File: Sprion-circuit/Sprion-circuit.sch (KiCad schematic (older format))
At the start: 0 parts

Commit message: Push, Push, Push
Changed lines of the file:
@@
 $EndDescr
 $Sheet
-S 1250 1500 2850 1250
+S 1400 1500 2850 1250
 U 60E26C28
 F0 "DRV8212" 50
 F1 "DRV8212.sch" 50
-F2 "MD1_IN1" I L 1250 1600 50
-F3 "MD1_IN2" I L 1250 1700 50
-F4 "MD1_OUT1" I R 4100 1600 50
-F5 "MD1_OUT2" I R 4100 1700 50
-F6 "MD1_CS" I L 1250 1800 50
-F7 "MD2_IN1" I L 1250 1950 50
-F8 "MD2_IN2" I L 1250 2050 50
-F9 "MD2_OUT1" I R 4100 1850 50
-F10 "MD2_OUT2" I R 4100 1950 50
-F11 "MD_SUC_IN1" I L 1250 2300 50
-F12 "MD_SUC_IN2" I L 1250 2400 50
-F13 "MD_SUC_OUT1" I R 4100 2100 50
-F14 "MD_SUC_OUT2" I R 4100 2200 50
-F15 "MD2_CS" I L 1250 2150 50
+F2 "MD1_IN1" I L 1400 1600 50
+F3 "MD1_IN2" I L 1400 1700 50
+F4 "MD1_OUT1" O R 4250 1600 50
+F5 "MD1_OUT2" O R 4250 1700 50
+F6 "MD1_CS" I L 1400 1800 50
+F7 "MD2_IN1" I L 1400 1950 50
+F8 "MD2_IN2" I L 1400 2050 50
+F9 "MD2_OUT1" O R 4250 1850 50
+F10 "MD2_OUT2" O R 4250 1950 50
+F11 "MD_SUC_IN1" I L 1400 2300 50
+F12 "MD_SUC_IN2" I L 1400 2400 50
+F13 "MD_SUC_OUT1" O R 4250 2100 50
+F14 "MD_SUC_OUT2" O R 4250 2200 50
+F15 "MD2_CS" I L 1400 2150 50
 $EndSheet
 $Sheet
@@
 F0 "Power" 50
 F1 "Power.sch" 50
-F2 "BAT" I L 1300 3950 50
+F2 "BAT" O L 1300 3950 50
 $EndSheet
 $Sheet

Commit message: wall sensor
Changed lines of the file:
@@
-$EndSheet
-$Sheet
-S 5200 2100 2600 2050
-U 60F363D5
-F0 "STM32f405" 50
-F1 "STM32f405.sch" 50
 $EndSheet
 $Sheet
@@
 F0 "wall_sensor" 50
 F1 "wall_sensor.sch" 50
+F2 "IRLED_SIDE" I L 8850 2900 50
+F3 "IRLED_FRONT" I L 8850 2750 50
+F4 "SENSOR_WALL_FR" O R 10700 2600 50
+F5 "SENSOR_WALL_FL" O R 10700 2750 50
+F6 "SENSOR_WALL_SR" O R 10700 2900 50
+F7 "SENSOR_WALL_SL" O R 10700 3050 50
+$EndSheet
+$Sheet
+S 5200 2100 2600 2050
+U 60F363D5
+F0 "Controller" 50
+F1 "Controller.sch" 50
 $EndSheet
 $EndSCHEMATC

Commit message: :fix　いろいろ
後で書きます
とりあえず寝ます
許してください
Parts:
- added J? (x2): Conn_02x03_Odd_Even, symbol Connector_Generic:Conn_02x03_Odd_Even
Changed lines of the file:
@@
 $Descr A4 11693 8268
 encoding utf-8
-Sheet 1 5
+Sheet 1 6
 Title ""
 Date ""
@@
 Comment4 ""
 $EndDescr
-$Sheet
-S 1400 1500 2850 1250
-U 60E26C28
-F0 "DRV8212" 50
-F1 "DRV8212.sch" 50
-F2 "MD1_IN1" I L 1400 1600 50
-F3 "MD1_IN2" I L 1400 1700 50
-F4 "MD1_OUT1" O R 4250 1600 50
-F5 "MD1_OUT2" O R 4250 1700 50
-F6 "MD1_CS" I L 1400 1800 50
-F7 "MD2_IN1" I L 1400 1950 50
-F8 "MD2_IN2" I L 1400 2050 50
-F9 "MD2_OUT1" O R 4250 1850 50
-F10 "MD2_OUT2" O R 4250 1950 50
-F11 "MD_SUC_IN1" I L 1400 2300 50
-F12 "MD_SUC_IN2" I L 1400 2400 50
-F13 "MD_SUC_OUT1" O R 4250 2100 50
-F14 "MD_SUC_OUT2" O R 4250 2200 50
-F15 "MD2_CS" I L 1400 2150 50
-$EndSheet
 $Sheet
 S 1300 3750 2100 1200
@@
 F7 "SENSOR_WALL_SL" O R 10700 3050 50
 $EndSheet
+$Comp
+L Connector_Generic:Conn_02x03_Odd_Even J?
+U 1 1 61A7CC1C
+P 5200 1050
+F 0 "J?" V 5204 1230 50  0000 L CNN
+F 1 "Conn_02x03_Odd_Even" V 5295 1230 50  0000 L CNN
+F 2 "" H 5200 1050 50  0001 C CNN
+F 3 "~" H 5200 1050 50  0001 C CNN
+	1    5200 1050
+	0    1    1    0
+$EndComp
+$Comp
+L Connector_Generic:Conn_02x03_Odd_Even J?
+U 1 1 61A7F0D6
+P 6600 1050
+F 0 "J?" V 6604 1230 50  0000 L CNN
+F 1 "Conn_02x03_Odd_Even" V 6695 1230 50  0000 L CNN
+F 2 "" H 6600 1050 50  0001 C CNN
+F 3 "~" H 6600 1050 50  0001 C CNN
+	1    6600 1050
+	0    1    1    0
+$EndComp
 $Sheet
-S 5200 2100 2600 2050
+S 1600 1850 2850 1250
+U 60E26C28
+F0 "DRV8212" 50
+F1 "DRV8212.sch" 50
+F2 "MD1_IN1" I L 1600 1950 50
+F3 "MD1_IN2" I L 1600 2050 50
+F4 "MD1_OUT1" O R 4450 1950 50
+F5 "MD1_OUT2" O R 4450 2050 50
+F6 "MD1_CS" I L 1600 2150 50
+F7 "MD2_IN1" I L 1600 2300 50
+F8 "MD2_IN2" I L 1600 2400 50
+F9 "MD2_OUT1" O R 4450 2200 50
+F10 "MD2_OUT2" O R 4450 2300 50
+F11 "MD_SUC_IN1" I L 1600 2650 50
+F12 "MD_SUC_IN2" I L 1600 2750 50
+F15 "MD2_CS" I L 1600 2500 50
+$EndSheet
+$Sheet
+S 5200 2050 2600 2050
 U 60F363D5
 F0 "Controller" 50
 F1 "Controller.sch" 50
+F2 "IMU_SCK" O R 7800 2150 50
+F3 "IMU_MISO" I R 7800 2250 50
+F4 "IMU_MOSI" O R 7800 2350 50
+F5 "ENCODER_1B" I R 7800 2600 50
+F6 "ENCODER_1A" I R 7800 2700 50
+F7 "IMU_CS" O R 7800 2450 50
+F8 "BATT" I R 7800 3000 50
+F9 "IRLED_FRONT" O R 7800 3200 50
+F10 "IRLED_SIDE" O R 7800 3300 50
+F11 "MD1_IN1" O R 7800 3500 50
+F12 "MD1_IN2" O R 7800 3600 50
+F13 "MD2_IN1" O L 5200 2250 50
+F14 "MD2_IN2" O L 5200 2350 50
+F15 "MD1_CS" I R 7800 3700 50
+F16 "MD2_CS" I L 5200 2450 50
+F17 "SENSOR_WALL_FR" I L 5200 2650 50
+F18 "SENSOR_WALL_FL" I L 5200 2750 50
+F19 "SENSOR_WALL_SR" I L 5200 2900 50
+F20 "SENSOR_WALL_SL" I L 5200 3000 50
+$EndSheet
+$Sheet
+S 5100 5350 1700 1150
+U 61A9F6C1
+F0 "IMU" 50
+F1 "IMU.sch" 50
+F2 "IMU_SDI" I L 5100 5550 50
+F3 "IMU_SDO" O L 5100 5700 50
+F4 "CS" I L 5100 5850 50
+F5 "IMU_INT" O L 5100 6000 50
+F6 "IMU_SPC" B L 5100 6150 50
 $EndSheet
 $EndSCHEMATC

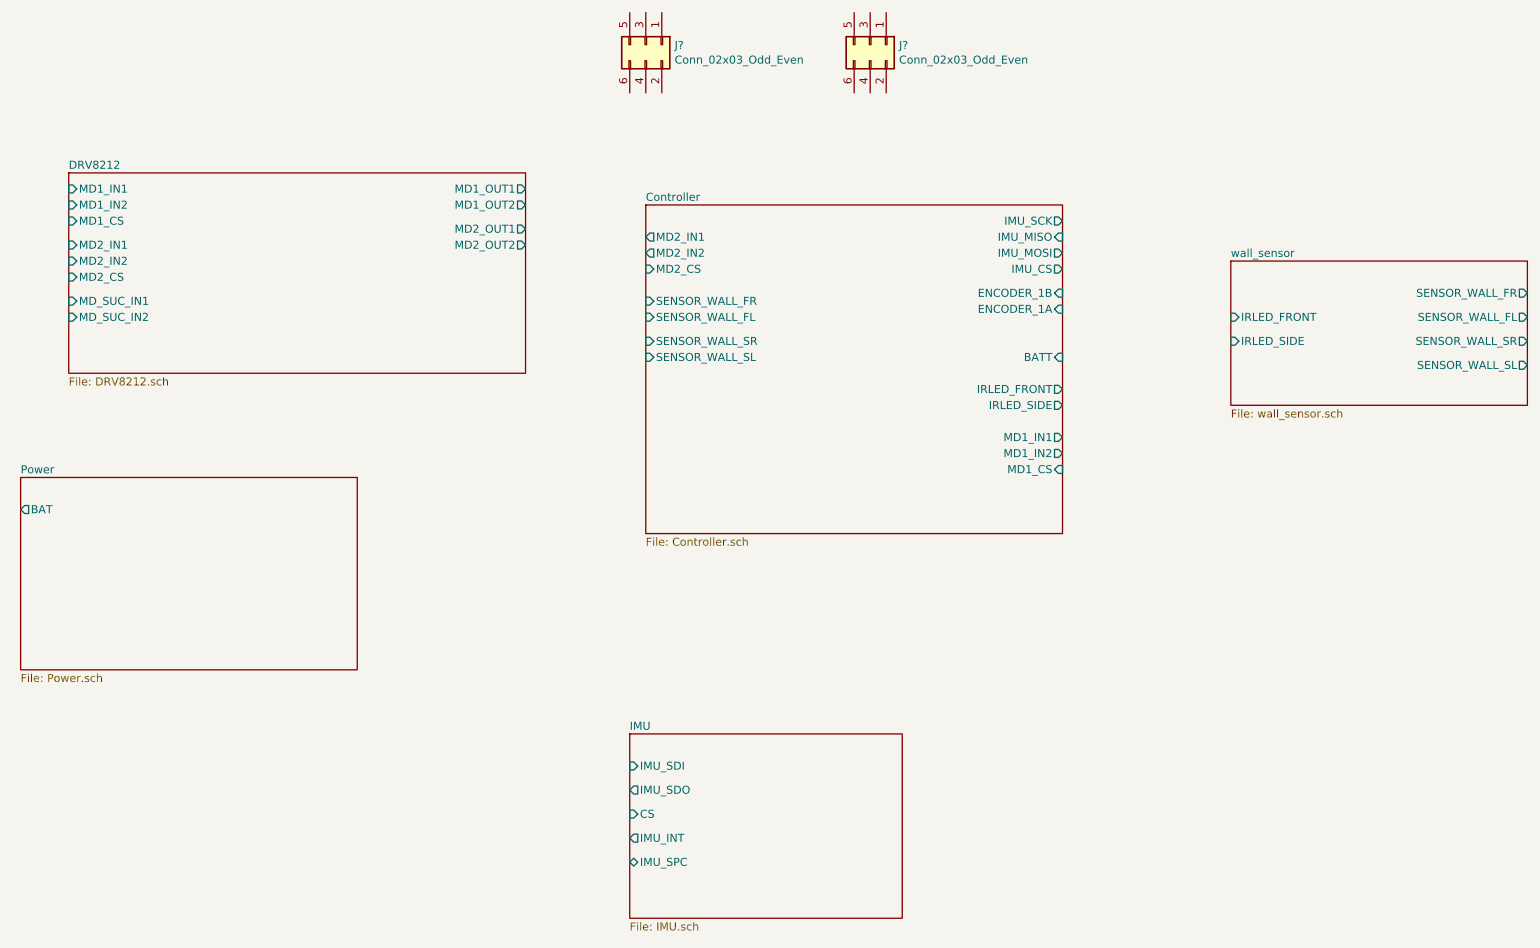
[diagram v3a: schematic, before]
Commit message: fix: MD周り,タイマー割り当て
MDの書き方を変えた
タイマー割り当てを再構成、対称性・高性能タイマーをどうするかみたいなとこ
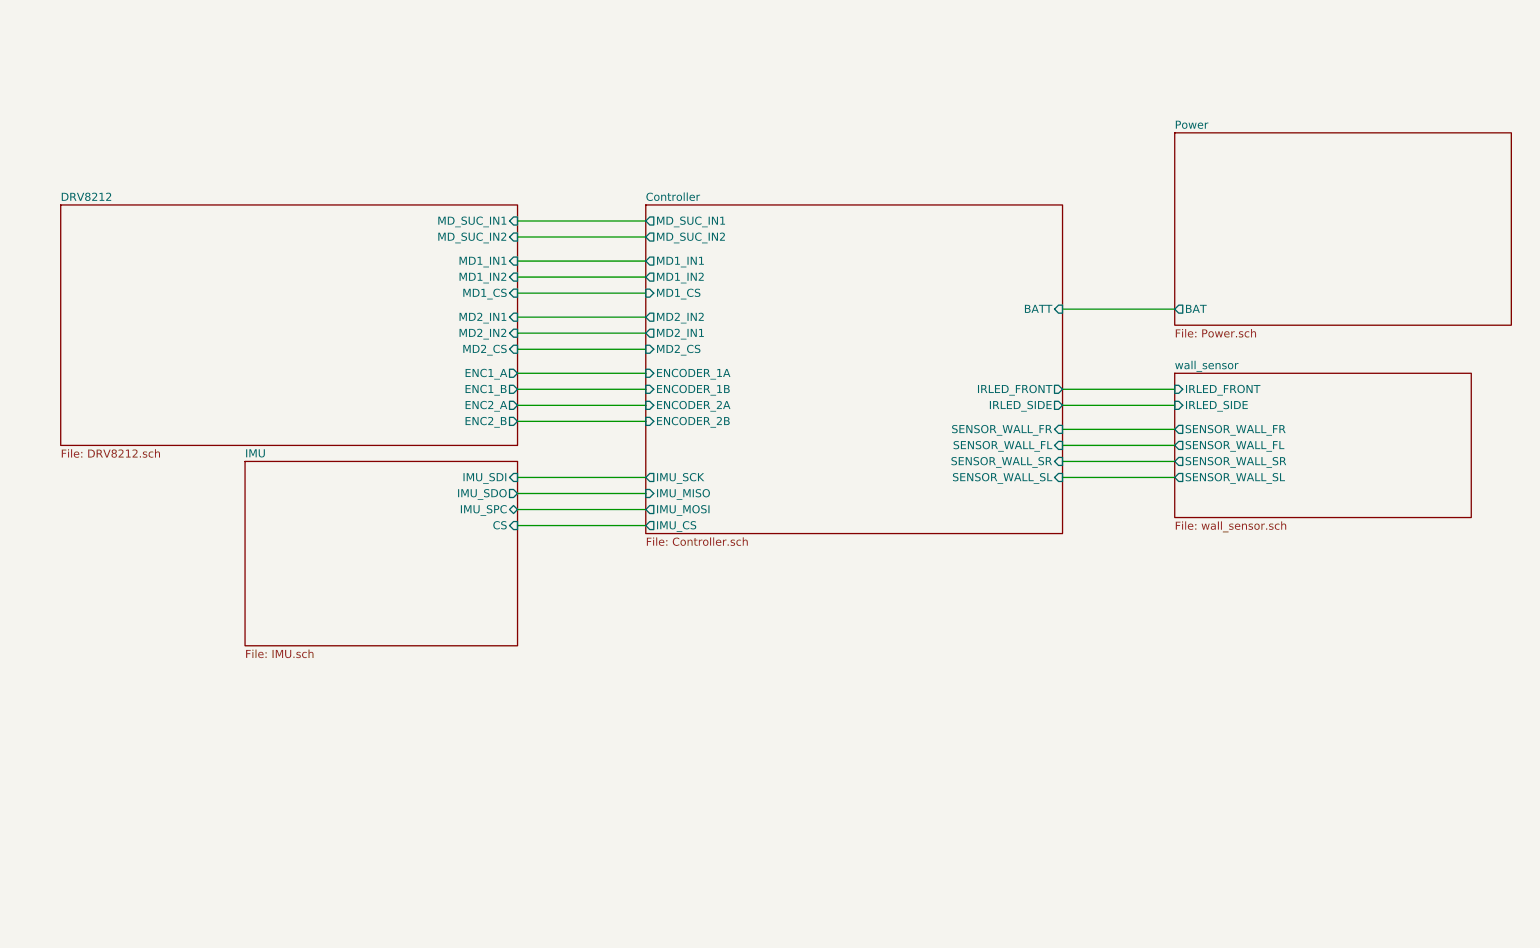
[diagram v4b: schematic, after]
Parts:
- removed J? (x2): Conn_02x03_Odd_Even, symbol Connector_Generic:Conn_02x03_Odd_Even
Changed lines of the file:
@@
 $EndDescr
 $Sheet
-S 1300 3750 2100 1200
+S 8500 1600 2100 1200
 U 60F3852A
 F0 "Power" 50
 F1 "Power.sch" 50
-F2 "BAT" O L 1300 3950 50
+F2 "BAT" O L 8500 2700 50
 $EndSheet
 $Sheet
-S 8850 2400 1850 900
+S 8500 3100 1850 900
 U 60E5E10A
 F0 "wall_sensor" 50
 F1 "wall_sensor.sch" 50
-F2 "IRLED_SIDE" I L 8850 2900 50
-F3 "IRLED_FRONT" I L 8850 2750 50
-F4 "SENSOR_WALL_FR" O R 10700 2600 50
-F5 "SENSOR_WALL_FL" O R 10700 2750 50
-F6 "SENSOR_WALL_SR" O R 10700 2900 50
-F7 "SENSOR_WALL_SL" O R 10700 3050 50
+F2 "IRLED_SIDE" I L 8500 3300 50
+F3 "IRLED_FRONT" I L 8500 3200 50
+F4 "SENSOR_WALL_FR" O L 8500 3450 50
+F5 "SENSOR_WALL_FL" O L 8500 3550 50
+F6 "SENSOR_WALL_SR" O L 8500 3650 50
+F7 "SENSOR_WALL_SL" O L 8500 3750 50
 $EndSheet
-$Comp
-L Connector_Generic:Conn_02x03_Odd_Even J?
-U 1 1 61A7CC1C
-P 5200 1050
-F 0 "J?" V 5204 1230 50  0000 L CNN
-F 1 "Conn_02x03_Odd_Even" V 5295 1230 50  0000 L CNN
-F 2 "" H 5200 1050 50  0001 C CNN
-F 3 "~" H 5200 1050 50  0001 C CNN
-	1    5200 1050
-	0    1    1    0
-$EndComp
-$Comp
-L Connector_Generic:Conn_02x03_Odd_Even J?
-U 1 1 61A7F0D6
-P 6600 1050
-F 0 "J?" V 6604 1230 50  0000 L CNN
-F 1 "Conn_02x03_Odd_Even" V 6695 1230 50  0000 L CNN
-F 2 "" H 6600 1050 50  0001 C CNN
-F 3 "~" H 6600 1050 50  0001 C CNN
-	1    6600 1050
-	0    1    1    0
-$EndComp
 $Sheet
-S 1600 1850 2850 1250
-U 60E26C28
-F0 "DRV8212" 50
-F1 "DRV8212.sch" 50
-F2 "MD1_IN1" I L 1600 1950 50
-F3 "MD1_IN2" I L 1600 2050 50
-F4 "MD1_OUT1" O R 4450 1950 50
-F5 "MD1_OUT2" O R 4450 2050 50
-F6 "MD1_CS" I L 1600 2150 50
-F7 "MD2_IN1" I L 1600 2300 50
-F8 "MD2_IN2" I L 1600 2400 50
-F9 "MD2_OUT1" O R 4450 2200 50
-F10 "MD2_OUT2" O R 4450 2300 50
-F11 "MD_SUC_IN1" I L 1600 2650 50
-F12 "MD_SUC_IN2" I L 1600 2750 50
-F15 "MD2_CS" I L 1600 2500 50
+S 2700 3650 1700 1150
+U 61A9F6C1
+F0 "IMU" 50
+F1 "IMU.sch" 50
+F2 "IMU_SDI" I R 4400 3750 50
+F3 "IMU_SDO" O R 4400 3850 50
+F4 "CS" I R 4400 4050 50
+F5 "IMU_SPC" B R 4400 3950 50
 $EndSheet
+Wire Wire Line
+	5200 2400 4400 2400
+Wire Wire Line
+	4400 2500 5200 2500
+Wire Wire Line
+	5200 2600 4400 2600
+Wire Wire Line
+	4400 2750 5200 2750
+Wire Wire Line
+	5200 2850 4400 2850
+Wire Wire Line
+	4400 2950 5200 2950
+Wire Wire Line
+	4400 2150 5200 2150
+Wire Wire Line
+	5200 2250 4400 2250
+Wire Wire Line
+	7800 3200 8500 3200
+Wire Wire Line
+	7800 3300 8500 3300
+Wire Wire Line
+	7800 3450 8500 3450
+Wire Wire Line
+	8500 3550 7800 3550
+Wire Wire Line
+	7800 3650 8500 3650
+Wire Wire Line
+	8500 3750 7800 3750
+Wire Wire Line
+	8500 2700 7800 2700
 $Sheet
 S 5200 2050 2600 2050
@@
 F0 "Controller" 50
 F1 "Controller.sch" 50
-F2 "IMU_SCK" O R 7800 2150 50
-F3 "IMU_MISO" I R 7800 2250 50
-F4 "IMU_MOSI" O R 7800 2350 50
-F5 "ENCODER_1B" I R 7800 2600 50
-F6 "ENCODER_1A" I R 7800 2700 50
-F7 "IMU_CS" O R 7800 2450 50
-F8 "BATT" I R 7800 3000 50
+F2 "IMU_SCK" O L 5200 3750 50
+F3 "IMU_MISO" I L 5200 3850 50
+F4 "IMU_MOSI" O L 5200 3950 50
+F5 "ENCODER_1B" I L 5200 3200 50
+F6 "ENCODER_1A" I L 5200 3100 50
+F7 "IMU_CS" O L 5200 4050 50
+F8 "BATT" I R 7800 2700 50
 F9 "IRLED_FRONT" O R 7800 3200 50
 F10 "IRLED_SIDE" O R 7800 3300 50
-F11 "MD1_IN1" O R 7800 3500 50
-F12 "MD1_IN2" O R 7800 3600 50
-F13 "MD2_IN1" O L 5200 2250 50
-F14 "MD2_IN2" O L 5200 2350 50
-F15 "MD1_CS" I R 7800 3700 50
-F16 "MD2_CS" I L 5200 2450 50
-F17 "SENSOR_WALL_FR" I L 5200 2650 50
-F18 "SENSOR_WALL_FL" I L 5200 2750 50
-F19 "SENSOR_WALL_SR" I L 5200 2900 50
-F20 "SENSOR_WALL_SL" I L 5200 3000 50
+F11 "MD1_IN1" O L 5200 2400 50
+F12 "MD1_IN2" O L 5200 2500 50
+F13 "MD2_IN1" O L 5200 2850 50
+F14 "MD2_IN2" O L 5200 2750 50
+F15 "MD1_CS" I L 5200 2600 50
+F16 "MD2_CS" I L 5200 2950 50
+F17 "SENSOR_WALL_FR" I R 7800 3450 50
+F18 "SENSOR_WALL_FL" I R 7800 3550 50
+F19 "SENSOR_WALL_SR" I R 7800 3650 50
+F20 "SENSOR_WALL_SL" I R 7800 3750 50
+F21 "MD_SUC_IN1" O L 5200 2150 50
+F22 "MD_SUC_IN2" O L 5200 2250 50
+F23 "ENCODER_2A" I L 5200 3300 50
+F24 "ENCODER_2B" I L 5200 3400 50
 $EndSheet
 $Sheet
-S 5100 5350 1700 1150
-U 61A9F6C1
-F0 "IMU" 50
-F1 "IMU.sch" 50
-F2 "IMU_SDI" I L 5100 5550 50
-F3 "IMU_SDO" O L 5100 5700 50
-F4 "CS" I L 5100 5850 50
-F5 "IMU_INT" O L 5100 6000 50
-F6 "IMU_SPC" B L 5100 6150 50
+S 1550 2050 2850 1500
+U 60E26C28
+F0 "DRV8212" 50
+F1 "DRV8212.sch" 50
+F2 "MD1_IN1" I R 4400 2400 50
+F3 "MD1_IN2" I R 4400 2500 50
+F4 "MD1_CS" I R 4400 2600 50
+F5 "MD2_IN1" I R 4400 2750 50
+F6 "MD2_IN2" I R 4400 2850 50
+F7 "MD_SUC_IN1" I R 4400 2150 50
+F8 "MD_SUC_IN2" I R 4400 2250 50
+F9 "MD2_CS" I R 4400 2950 50
+F10 "ENC1_A" O R 4400 3100 50
+F11 "ENC1_B" O R 4400 3200 50
+F12 "ENC2_A" O R 4400 3300 50
+F13 "ENC2_B" O R 4400 3400 50
 $EndSheet
+Wire Wire Line
+	5200 3750 4400 3750
+Wire Wire Line
+	4400 3850 5200 3850
+Wire Wire Line
+	5200 3950 4400 3950
+Wire Wire Line
+	4400 4050 5200 4050
+Wire Wire Line
+	4400 3100 5200 3100
+Wire Wire Line
+	5200 3200 4400 3200
+Wire Wire Line
+	4400 3300 5200 3300
+Wire Wire Line
+	5200 3400 4400 3400
 $EndSCHEMATC

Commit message: add,feat,fix:すまんコミットわすれててぐちゃぐちゃや
配置始めた。
フットプリント割り当てた
回路図pdfで吐いた
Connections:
- no-connect marks 0 -> 1
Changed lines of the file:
@@
 Wire Wire Line
 	5200 3400 4400 3400
+NoConn ~ 10000 2050
 $EndSCHEMATC

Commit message: add fix feat: でけたー（コミットしてなくてごめん）
ベタ塗、配線、再配置等
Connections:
- no-connect marks 1 -> 0
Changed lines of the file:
@@
 $EndDescr
-$Sheet
-S 8500 1600 2100 1200
-U 60F3852A
-F0 "Power" 50
-F1 "Power.sch" 50
-F2 "BAT" O L 8500 2700 50
-$EndSheet
 $Sheet
 S 8500 3100 1850 900
@@
 Wire Wire Line
 	5200 3400 4400 3400
-NoConn ~ 10000 2050
+$Sheet
+S 8500 1600 2100 1200
+U 60F3852A
+F0 "Power" 50
+F1 "Power.sch" 50
+F2 "BAT" O L 8500 2700 50
+$EndSheet
 $EndSCHEMATC
